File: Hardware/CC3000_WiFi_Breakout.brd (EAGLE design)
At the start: 25.4 x 45.7 mm, 31 parts, among them J1 U.FL, U1 LM1117, U3 74HC4050, U5 CC3000

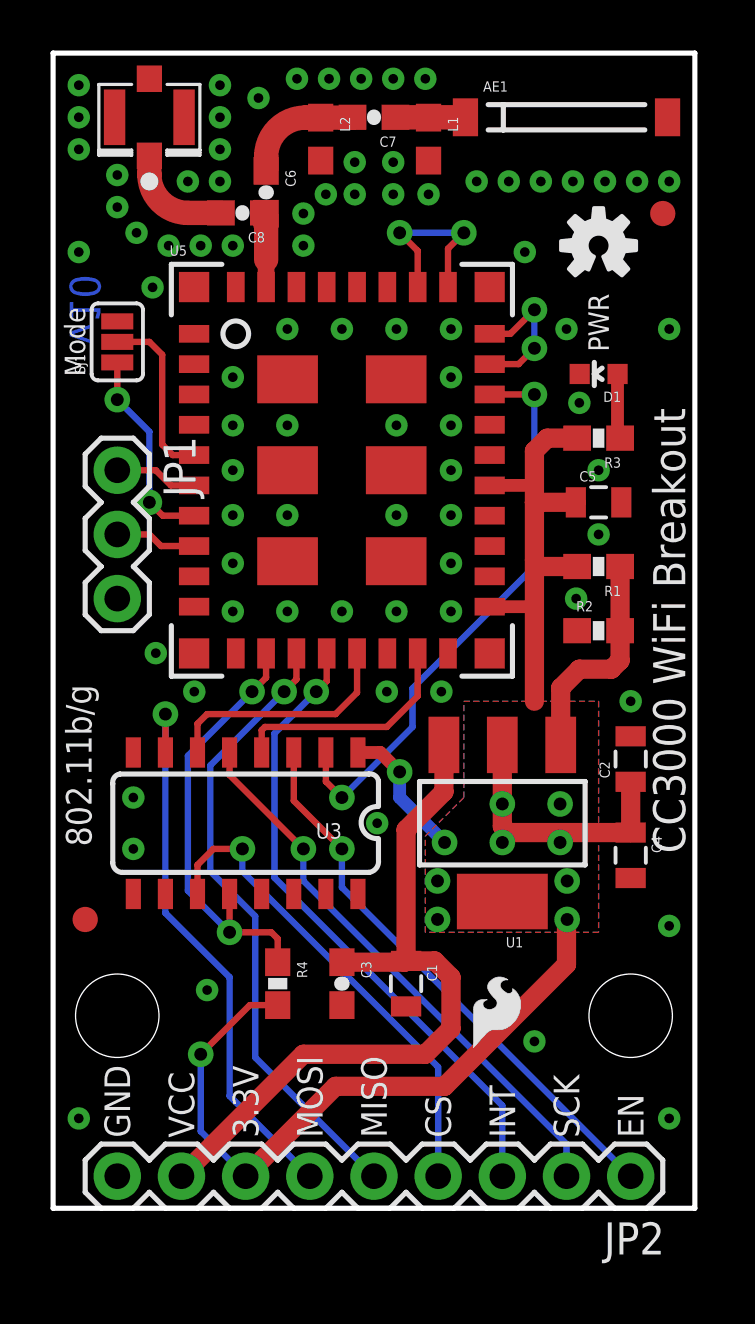
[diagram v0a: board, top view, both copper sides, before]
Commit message: Added silk U.FL; adjusted tvalue markings for easier reading
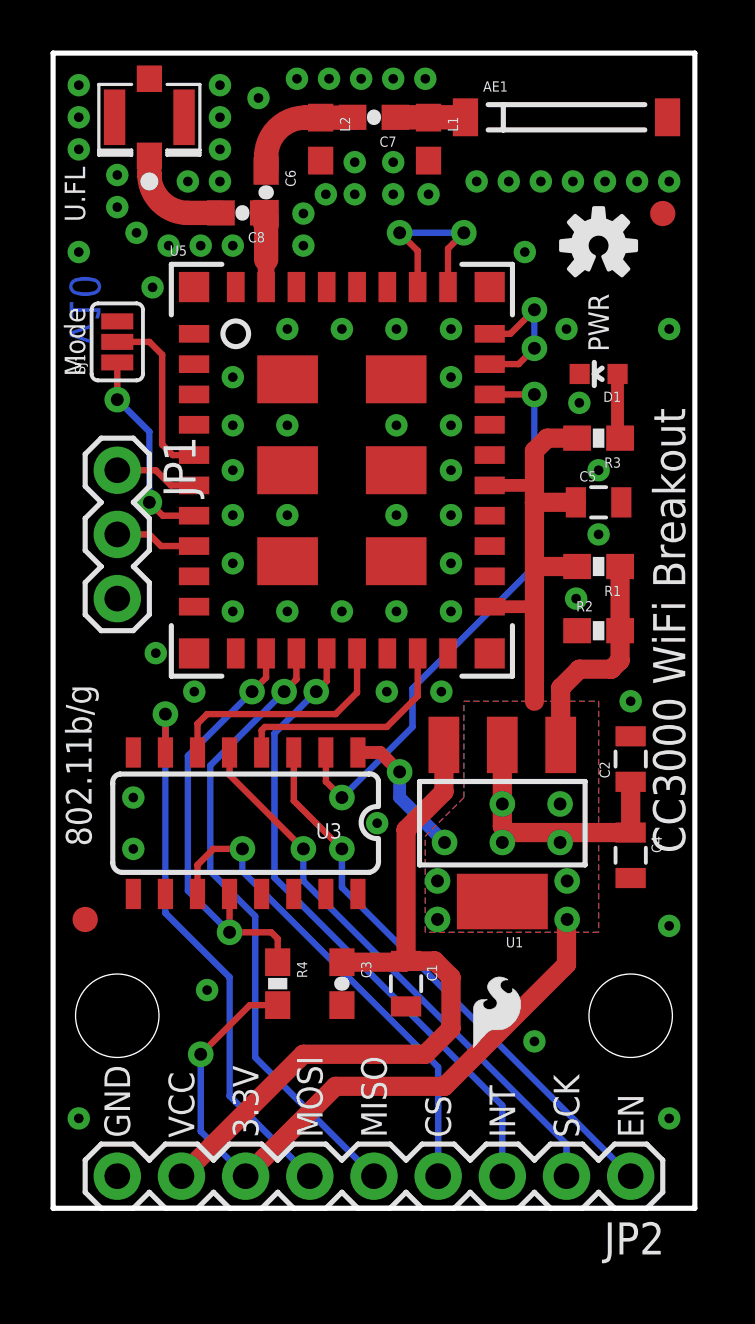
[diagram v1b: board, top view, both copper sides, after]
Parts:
- L1: value (none) -> DNP
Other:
- board text added: "U.FL"
